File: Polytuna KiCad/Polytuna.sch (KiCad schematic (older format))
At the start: 43 parts, among them IC1 AP7313-33SAG-7, J1 Barrel_Jack, J2 Conn_01x02, J3 Conn_01x02, J4 Conn_01x04, SW1 SW_Push, SW2 SW_Push, SW3 SW_Push, SW4 SW_DPDT_x2, U1 LM358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

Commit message: PCB v0.1
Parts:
- removed J?: Audio-Jack-3, symbol Audio-Jack-3
- removed J?: Audio-Jack-3, def-footprints:CONN_Jack_Female_6.35mm_THD, symbol Audio-Jack-3
- removed SW4: SW_DPDT_x2, def-footprints:Switches_Stomp_Switch_3PDT, symbol SW_DPDT_x2
- added Input1, Output1: JACK_FEMALE_STEREO_6_PINS, def-footprints:CONN_Jack_Female_6.35mm_THD, symbol JACK_FEMALE_STEREO_6_PINS
- added J5: Conn_01x02, Pin_Headers:Pin_Header_Straight_1x02_Pitch2.54mm, symbol Conn_01x02
- added SW4: SW_TPDT, footprints:IceStomp_Switch_3PDT, symbol SW_TPDT
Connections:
- net labels added: DC_Conv, INPUT, InputStage, Output, PowerIn
- wire segments 144 -> 157
- no-connect marks 17 -> 18
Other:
- moved on the sheet: C1, C2, U3

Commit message: PCB v0.1
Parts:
- added JMP2: 2Jumper, def-footprints:Miscellaneous_Solder_Jumper, symbol 2Jumper
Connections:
- net GND: now also JMP2.2
- net GNDA: now also JMP2.1
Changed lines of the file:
@@
 Wire Wire Line
 	6200 2250 6000 2250
+$Comp
+L 2Jumper JMP2
+U 1 1 5AB0FC19
+P 1050 7500
+F 0 "JMP2" H 1050 7595 60  0000 C CNN
+F 1 "2Jumper" H 1050 7685 60  0001 C CNN
+F 2 "def-footprints:Miscellaneous_Solder_Jumper" H 2205 7570 60  0001 C CNN
+F 3 "" H 2205 7570 60  0000 C CNN
+	1    1050 7500
+	-1   0    0    1
+$EndComp
+Wire Wire Line
+	850  7500 800  7500
+Connection ~ 800  7500
+Wire Wire Line
+	1250 7500 1250 7500
+Connection ~ 1250 7500
 $EndSCHEMATC

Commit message: Some fixes
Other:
- moved on the sheet: BOARD1, BT1, C1, C2, C3, C4, C5, C6, C7, C8, Ct1, D1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

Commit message: Changed OP's footprint
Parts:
- U1: footprint Housings_SOIC:SOIC-8-1EP_3.9x4.9mm_Pitch1.27mm -> Housings_SOIC:SOIC-8_3.9x4.9mm_Pitch1.27mm
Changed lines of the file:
@@
 LIBS:contrib
 LIBS:valves
+LIBS:SparkFun-Connectors
+LIBS:SparkFun-Copper
+LIBS:SparkFun-IC-Analog
+LIBS:SparkFun-IC-Logic
+LIBS:SparkFun-IC-Memory
+LIBS:SparkFun-IC-PMIC
+LIBS:SparkFun-Jacks
+LIBS:SparkFun-Mounting
+LIBS:SparkFun-Opto
+LIBS:kicad-library
+LIBS:teensy_3_2_full
+LIBS:pot_with_shield
+LIBS:switch_dpdt
+LIBS:ws2812b
+LIBS:AP7313-33SAG-7
+LIBS:dynamixel_conn_3
+LIBS:jack_female_mono
+LIBS:jack_female_mono_3_pins
+LIBS:jack_female_stereo_3_pins
+LIBS:jack_female_stereo_5_pins
+LIBS:jack_female_stereo_6_pins
+LIBS:usb-female
+LIBS:icescreamer_SW
+LIBS:sw_tpdt
 LIBS:Polytuna-cache
 EELAYER 25 0
@@
 F 0 "U1" H 6400 3700 50  0000 L CNN
 F 1 "LM358" H 6400 3300 50  0000 L CNN
-F 2 "Housings_SOIC:SOIC-8-1EP_3.9x4.9mm_Pitch1.27mm" H 6400 3500 50  0001 C CNN
+F 2 "Housings_SOIC:SOIC-8_3.9x4.9mm_Pitch1.27mm" H 6400 3500 50  0001 C CNN
 F 3 "" H 6400 3500 50  0001 C CNN
 	1    6400 3500

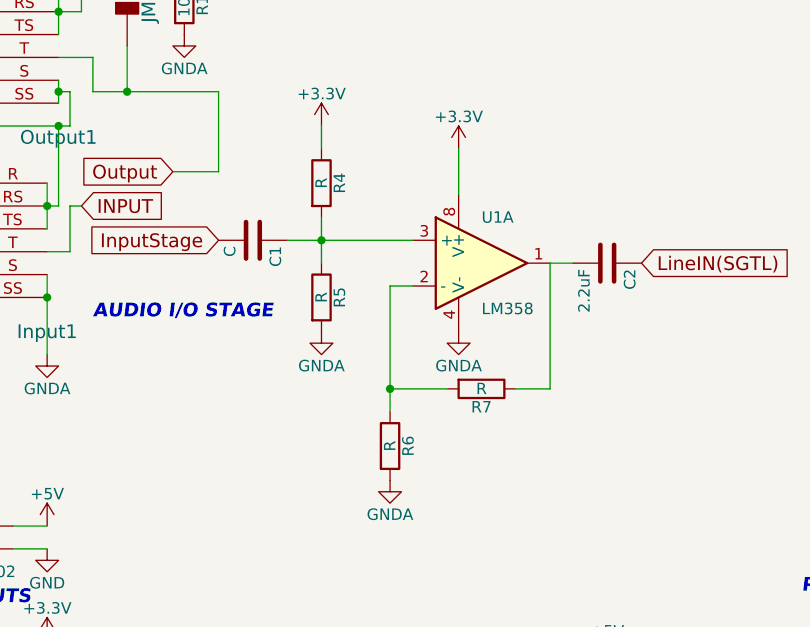
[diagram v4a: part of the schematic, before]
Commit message: Added values for input stage resistors
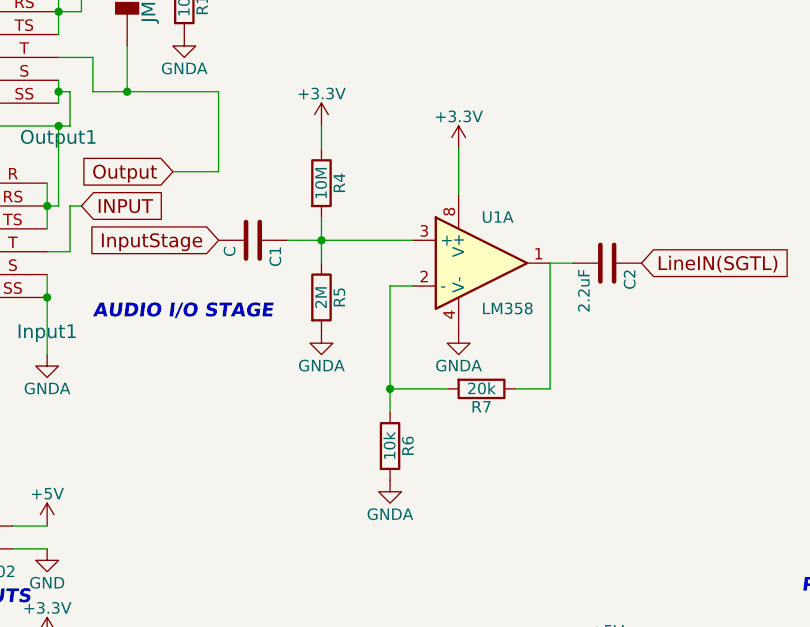
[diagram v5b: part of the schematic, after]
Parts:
- R4: value R -> 10M
- R5: value R -> 2M
- R6: value R -> 10k
- R7: value R -> 20k
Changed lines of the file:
@@
 P 6000 4300
 F 0 "R6" V 6080 4300 50  0000 C CNN
-F 1 "R" V 6000 4300 50  0000 C CNN
+F 1 "10k" V 6000 4300 50  0000 C CNN
 F 2 "Resistors_SMD:R_0805" V 5930 4300 50  0001 C CNN
 F 3 "" H 6000 4300 50  0001 C CNN
@@
 P 5700 3650
 F 0 "R5" V 5780 3650 50  0000 C CNN
-F 1 "R" V 5700 3650 50  0000 C CNN
+F 1 "2M" V 5700 3650 50  0000 C CNN
 F 2 "Resistors_SMD:R_0805" V 5630 3650 50  0001 C CNN
 F 3 "" H 5700 3650 50  0001 C CNN
@@
 P 6400 4050
 F 0 "R7" V 6480 4050 50  0000 C CNN
-F 1 "R" V 6400 4050 50  0000 C CNN
+F 1 "20k" V 6400 4050 50  0000 C CNN
 F 2 "Resistors_SMD:R_0805" V 6330 4050 50  0001 C CNN
 F 3 "" H 6400 4050 50  0001 C CNN
@@
 P 5700 3150
 F 0 "R4" V 5780 3150 50  0000 C CNN
-F 1 "R" V 5700 3150 50  0000 C CNN
+F 1 "10M" V 5700 3150 50  0000 C CNN
 F 2 "Resistors_SMD:R_0805" V 5630 3150 50  0001 C CNN
 F 3 "" H 5700 3150 50  0001 C CNN

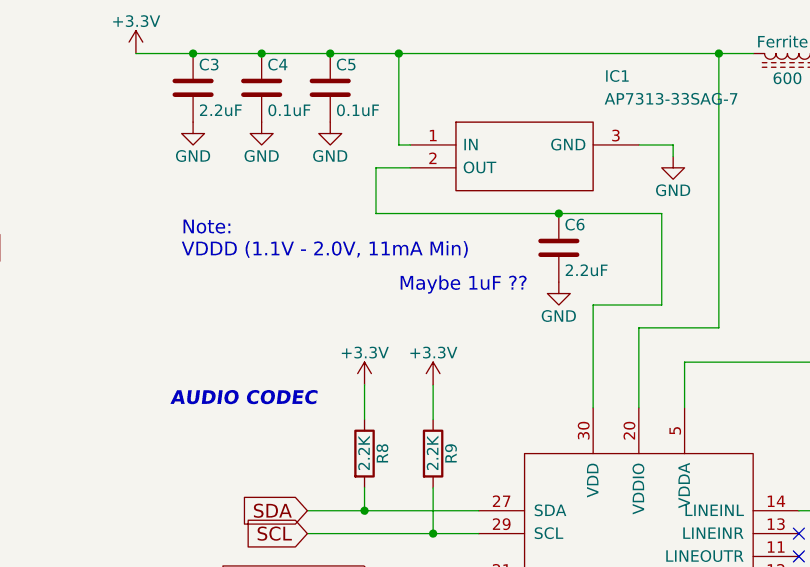
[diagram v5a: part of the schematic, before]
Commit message: Corrected C6 value
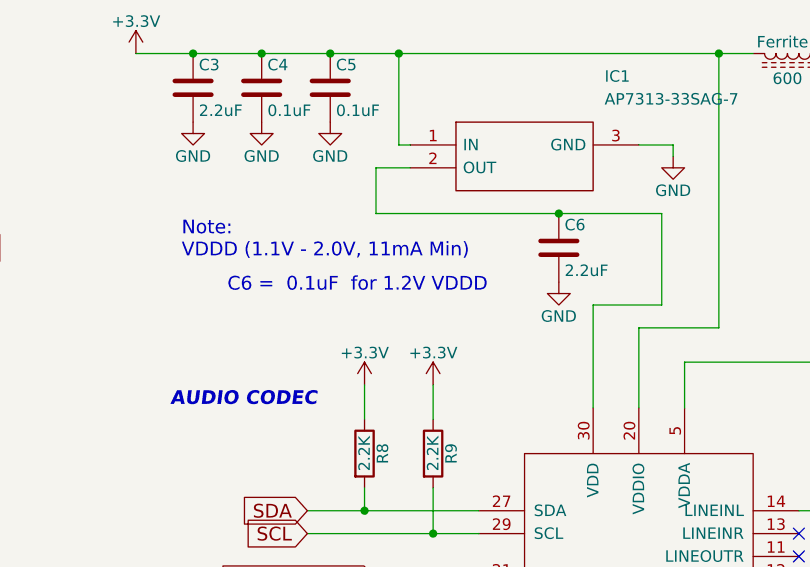
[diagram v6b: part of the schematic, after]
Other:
- note added: "C6 = 0.1uF for 1.2V VDDD"
- note removed: "Maybe 1uF ??"
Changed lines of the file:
@@
 	1    0    0    -1
 $EndComp
-Text Notes 11100 3300 0    60   ~ 0
-Maybe 1uF ??
+Text Notes 10350 3300 0    60   ~ 0
+C6 =  0.1uF  for 1.2V VDDD
 Wire Wire Line
 	4550 7500 4950 7500
